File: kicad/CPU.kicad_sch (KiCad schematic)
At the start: 37 parts, among them J1 Conn_ARM_SWD_TagConnect_TC203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, J2 Screw_Terminal_01x03, J3 Screw_Terminal_01x03, SW1 SW_Push, U7 STM32F303CBTx, U8 ATA6560-GAQW-N, Y1 8 MHz

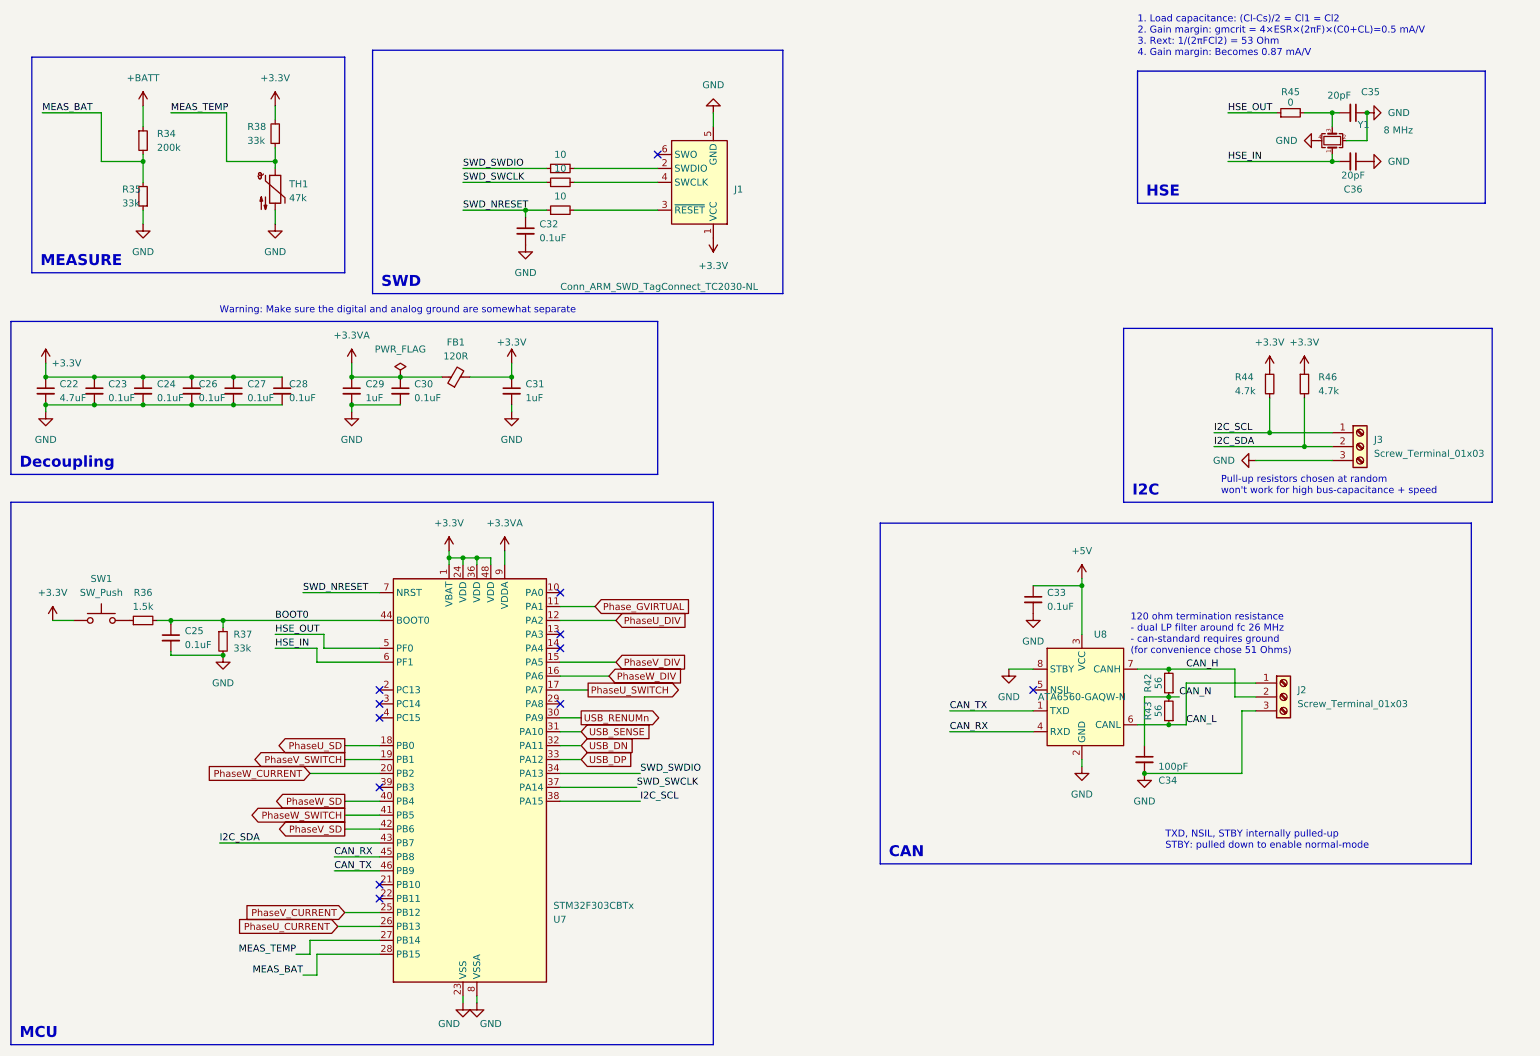
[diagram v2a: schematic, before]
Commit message: [kicad] Added different ESD protection device, silkscreen indication on the back, [review] Added pdf file and images of the front and back as well as 3d images
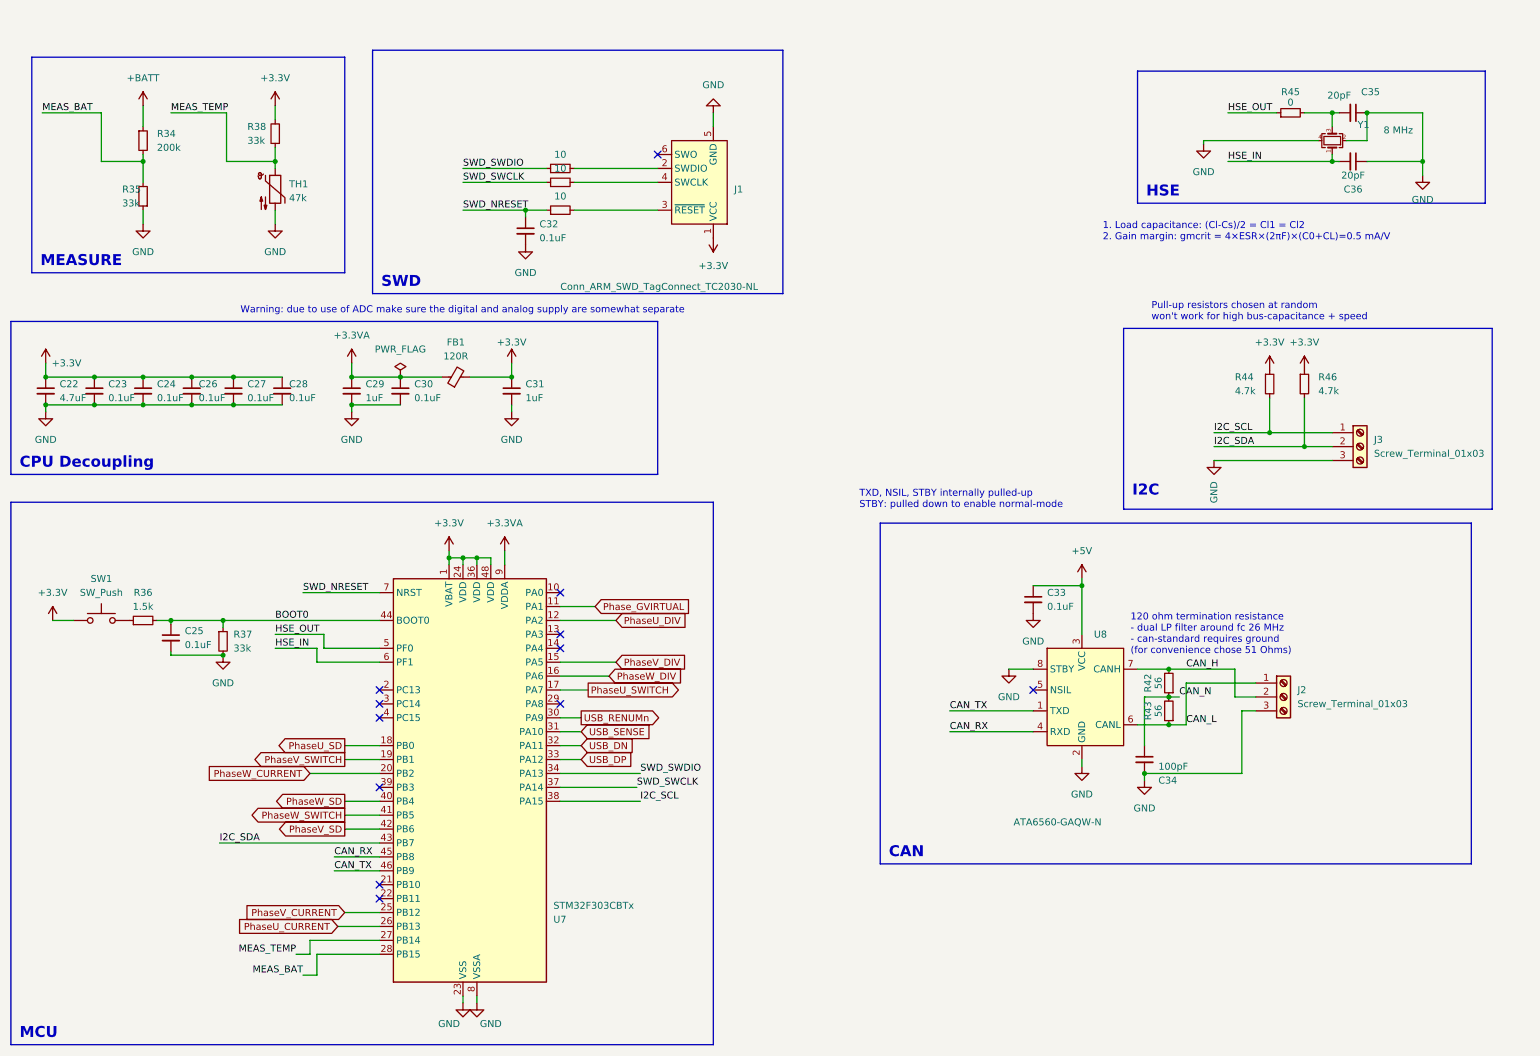
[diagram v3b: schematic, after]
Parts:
- R45: footprint Resistor_SMD:R_0402_1005Metric -> Resistor_SMD:R_0402_1005Metric_Pad0.72x0.64mm_HandSolder
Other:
- note added: "1. Load capacitance: (Cl-Cs)/2 = Cl1 = Cl2 2. Gain margin: gmcrit = 4×ESR×(2πF)×(C0+CL)=0.5 mA/V"
- note added: "Warning: due to use of ADC make sure the digital and analog supply are somewhat separate"
- note removed: "1. Load capacitance: (Cl-Cs)/2 = Cl1 = Cl2 2. Gain margin: gmcrit = 4×ESR×(2πF)×(C0+CL)=0.5 mA/V 3. Rext: 1/(2πFCl2) = 53 Ohm 4. Gain margin: Becomes 0.87 mA/V"
- note removed: "Warning: Make sure the digital and analog ground are somewhat separate"
- company: Igor Wolfs -> IW
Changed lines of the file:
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@@
     (title "BLDC Driver Project")
     (rev "1.0")
-    (company "Igor Wolfs")
+    (company "IW")
   )
   (junction (at 225.425 137.16) (diameter 0) (color 0 0 0 0)
+  )
+  (junction (at 271.78 34.29) (diameter 0) (color 0 0 0 0)
   )
   (junction (at 52.705 124.46) (diameter 0) (color 0 0 0 0)
@@
     (stroke (width 0) (type default))
   )
+  (wire (pts (xy 271.78 34.29) (xy 271.78 25.4))
+    (stroke (width 0) (type default))
+  )
   (wire (pts (xy 255.27 34.29) (xy 255.27 33.02))
     (stroke (width 0) (type default))
@@
     (stroke (width 0) (type default))
   )
+  (wire (pts (xy 231.775 30.48) (xy 231.775 31.115))
+    (stroke (width 0) (type default))
+  )
   (wire (pts (xy 243.84 83.82) (xy 255.27 83.82))
     (stroke (width 0) (type default))
@@
     (stroke (width 0) (type default))
   )
-  (wire (pts (xy 241.3 88.9) (xy 255.27 88.9))
+  (wire (pts (xy 233.68 88.9) (xy 255.27 88.9))
     (stroke (width 0) (type default))
   )
@@
     (stroke (width 0) (type default))
   )
+  (wire (pts (xy 271.78 25.4) (xy 261.62 25.4))
+    (stroke (width 0) (type default))
+  )
   (wire (pts (xy 38.1 73.66) (xy 46.99 73.66))
     (stroke (width 0) (type default))
@@
     (stroke (width 0) (type default))
   )
+  (wire (pts (xy 261.62 34.29) (xy 271.78 34.29))
+    (stroke (width 0) (type default))
+  )
   (wire (pts (xy 53.34 25.4) (xy 53.34 34.29))
     (stroke (width 0) (type default))
@@
     (stroke (width 0) (type default))
   )
+  (wire (pts (xy 271.78 36.83) (xy 271.78 34.29))
+    (stroke (width 0) (type default))
+  )
   (wire (pts (xy 68.58 179.07) (xy 66.04 179.07))
     (stroke (width 0) (type default))
@@
     (stroke (width 0) (type default))
   )
+  (wire (pts (xy 231.775 30.48) (xy 252.73 30.48))
+    (stroke (width 0) (type default))
+  )
   (wire (pts (xy 209.55 110.49) (xy 209.55 111.76))
     (stroke (width 0) (type default))
@@
     (stroke (width 0) (type default))
   )
+  (wire (pts (xy 220.98 147.32) (xy 220.98 146.05))
+    (stroke (width 0) (type default))
+  )
   (wire (pts (xy 74.93 156.21) (xy 81.28 156.21))
     (stroke (width 0) (type default))
@@
     (fill (type none))
   )
-  (rectangle (start 217.17 64.77) (end 284.48 96.52)
+  (rectangle (start 217.17 64.77) (end 284.48 97.79)
     (stroke (width 0) (type default))
     (fill (type none))
@@
     (effects (font (size 2 2) (thickness 2) bold) (justify left top))
   )
-  (text_box "Decoupling\n"
-    (at 13.97 86.36 0) (size 20.32 5.08)
+  (text_box "CPU Decoupling\n"
+    (at 13.97 86.36 0) (size 35.56 5.08)
     (stroke (width -0.0001) (type default))
     (fill (type none))
@@
   )
   (text "TXD, NSIL, STBY internally pulled-up\nSTBY: pulled down to enable normal-mode"
-    (at 224.79 160.02 0)
+    (at 168.91 97.79 0)
     (effects (font (size 1.27 1.27)) (justify left bottom))
   )
   (text "Pull-up resistors chosen at random\nwon't work for high bus-capacitance + speed"
-    (at 234.95 95.25 0)
-    (effects (font (size 1.27 1.27)) (justify left bottom))
-  )
-  (text "1. Load capacitance: (Cl-Cs)/2 = Cl1 = Cl2\n2. Gain margin: gmcrit = 4×ESR×(2πF)×(C0+CL)=0.5 mA/V\n3. Rext: 1/(2πFCl2) = 53 Ohm\n4. Gain margin: Becomes 0.87 mA/V\n"
-    (at 219.71 15.24 0)
-    (effects (font (size 1.27 1.27)) (justify left bottom))
-  )
-  (text "Warning: Make sure the digital and analog ground are somewhat separate\n"
-    (at 52.07 62.23 0)
+    (at 222.25 63.5 0)
+    (effects (font (size 1.27 1.27)) (justify left bottom))
+  )
+  (text "1. Load capacitance: (Cl-Cs)/2 = Cl1 = Cl2\n2. Gain margin: gmcrit = 4×ESR×(2πF)×(C0+CL)=0.5 mA/V"
+    (at 213.36 48.895 0)
+    (effects (font (size 1.27 1.27)) (justify left bottom))
+  )
+  (text "Warning: due to use of ADC make sure the digital and analog supply are somewhat separate\n"
+    (at 55.88 62.23 0)
     (effects (font (size 1.27 1.27)) (justify left bottom))
   )
@@
     )
   )
-  (symbol (lib_id "power:GND") (at 241.3 88.9 270) (unit 1)
+  (symbol (lib_id "power:GND") (at 233.68 88.9 0) (unit 1)
     (in_bom yes) (on_board yes) (dnp no)
-    (property "Reference" "#PWR053" (at 234.95 88.9 0)
-      (effects (font (size 1.27 1.27)) hide)
-    )
-    (property "Value" "GND" (at 237.49 88.9 90)
+    (property "Reference" "#PWR053" (at 233.68 95.25 0)
+      (effects (font (size 1.27 1.27)) hide)
+    )
+    (property "Value" "GND" (at 233.68 92.71 90)
       (effects (font (size 1.27 1.27)) (justify right))
     )
-    (property "Footprint" "" (at 241.3 88.9 0)
-      (effects (font (size 1.27 1.27)) hide)
-    )
-    (property "Datasheet" "" (at 241.3 88.9 0)
+    (property "Footprint" "" (at 233.68 88.9 0)
+      (effects (font (size 1.27 1.27)) hide)
+    )
+    (property "Datasheet" "" (at 233.68 88.9 0)
       (effects (font (size 1.27 1.27)) hide)
     )
@@
     )
   )
-  (symbol (lib_id "power:GND") (at 220.98 146.05 0) (unit 1)
-    (in_bom yes) (on_board yes) (dnp no) (fields_autoplaced)
-    (property "Reference" "#PWR052" (at 220.98 152.4 0)
-      (effects (font (size 1.27 1.27)) hide)
-    )
-    (property "Value" "GND" (at 220.98 151.13 0)
-      (effects (font (size 1.27 1.27)))
-    )
-    (property "Footprint" "" (at 220.98 146.05 0)
-      (effects (font (size 1.27 1.27)) hide)
-    )
-    (property "Datasheet" "" (at 220.98 146.05 0)
+  (symbol (lib_id "power:GND") (at 220.98 147.32 0) (unit 1)
+    (in_bom yes) (on_board yes) (dnp no) (fields_autoplaced)
+    (property "Reference" "#PWR052" (at 220.98 153.67 0)
+      (effects (font (size 1.27 1.27)) hide)
+    )
+    (property "Value" "GND" (at 220.98 152.4 0)
+      (effects (font (size 1.27 1.27)))
+    )
+    (property "Footprint" "" (at 220.98 147.32 0)
+      (effects (font (size 1.27 1.27)) hide)
+    )
+    (property "Datasheet" "" (at 220.98 147.32 0)
       (effects (font (size 1.27 1.27)) hide)
     )
@@
   )
   (symbol (lib_id "bldc:ATA6560") (at 209.55 132.08 0) (unit 1)
-    (in_bom yes) (on_board yes) (dnp no) (fields_autoplaced)
+    (in_bom yes) (on_board yes) (dnp no)
     (property "Reference" "U8" (at 211.7441 120.65 0)
       (effects (font (size 1.27 1.27)) (justify left))
     )
-    (property "Value" "ATA6560-GAQW-N" (at 209.55 132.08 0)
+    (property "Value" "ATA6560-GAQW-N" (at 205.105 154.94 0)
       (effects (font (size 1.27 1.27)))
     )
@@
     )
   )
-  (symbol (lib_id "power:GND") (at 261.62 25.4 90) (unit 1)
-    (in_bom yes) (on_board yes) (dnp no) (fields_autoplaced)
-    (property "Reference" "#PWR057" (at 267.97 25.4 0)
-      (effects (font (size 1.27 1.27)) hide)
-    )
-    (property "Value" "GND" (at 265.43 25.4 90)
-      (effects (font (size 1.27 1.27)) (justify right))
-    )
-    (property "Footprint" "" (at 261.62 25.4 0)
-      (effects (font (size 1.27 1.27)) hide)
-    )
-    (property "Datasheet" "" (at 261.62 25.4 0)
+  (symbol (lib_id "power:GND") (at 271.78 36.83 0) (unit 1)
+    (in_bom yes) (on_board yes) (dnp no) (fields_autoplaced)
+    (property "Reference" "#PWR057" (at 271.78 43.18 0)
+      (effects (font (size 1.27 1.27)) hide)
+    )
+    (property "Value" "GND" (at 271.78 41.275 0)
+      (effects (font (size 1.27 1.27)))
+    )
+    (property "Footprint" "" (at 271.78 36.83 0)
+      (effects (font (size 1.27 1.27)) hide)
+    )
+    (property "Datasheet" "" (at 271.78 36.83 0)
       (effects (font (size 1.27 1.27)) hide)
     )
@@
     )
   )
-  (symbol (lib_id "power:GND") (at 252.73 30.48 270) (unit 1)
-    (in_bom yes) (on_board yes) (dnp no) (fields_autoplaced)
-    (property "Reference" "#PWR056" (at 246.38 30.48 0)
-      (effects (font (size 1.27 1.27)) hide)
-    )
-    (property "Value" "GND" (at 248.92 30.48 90)
-      (effects (font (size 1.27 1.27)) (justify right))
-    )
-    (property "Footprint" "" (at 252.73 30.48 0)
-      (effects (font (size 1.27 1.27)) hide)
-    )
-    (property "Datasheet" "" (at 252.73 30.48 0)
+  (symbol (lib_id "power:GND") (at 231.775 31.115 0) (unit 1)
+    (in_bom yes) (on_board yes) (dnp no) (fields_autoplaced)
+    (property "Reference" "#PWR056" (at 231.775 37.465 0)
+      (effects (font (size 1.27 1.27)) hide)
+    )
+    (property "Value" "GND" (at 231.775 36.195 0)
+      (effects (font (size 1.27 1.27)))
+    )
+    (property "Footprint" "" (at 231.775 31.115 0)
+      (effects (font (size 1.27 1.27)) hide)
+    )
+    (property "Datasheet" "" (at 231.775 31.115 0)
       (effects (font (size 1.27 1.27)) hide)
     )
@@
     )
   )
-  (symbol (lib_id "power:GND") (at 261.62 34.29 90) (unit 1)
-    (in_bom yes) (on_board yes) (dnp no) (fields_autoplaced)
-    (property "Reference" "#PWR058" (at 267.97 34.29 0)
-      (effects (font (size 1.27 1.27)) hide)
-    )
-    (property "Value" "GND" (at 265.43 34.29 90)
-      (effects (font (size 1.27 1.27)) (justify right))
-    )
-    (property "Footprint" "" (at 261.62 34.29 0)
-      (effects (font (size 1.27 1.27)) hide)
-    )
-    (property "Datasheet" "" (at 261.62 34.29 0)
-      (effects (font (size 1.27 1.27)) hide)
-    )
-    (pin "1")
-    (instances
-      (project "bldc_project"
-        (path "/91e2f46a-700b-4d7a-a06a-22469f63223f/7eb1e86b-8a48-408f-b231-0c52f4ea1971"
-          (reference "#PWR058") (unit 1)
-        )
-      )
-    )
-  )
   (symbol (lib_id "power:GND") (at 142.24 25.4 180) (unit 1)
     (in_bom yes) (on_board yes) (dnp no) (fields_autoplaced)
@@
       (effects (font (size 1.27 1.27)))
     )
-    (property "Footprint" "Resistor_SMD:R_0402_1005Metric" (at 247.65 25.4 0)
-      (effects (font (size 1.27 1.27)) hide)
-    )
+    (property "Footprint" "Resistor_SMD:R_0402_1005Metric_Pad0.72x0.64mm_HandSolder" (at 247.65 25.4 0)
+      (effects (font (size 1.27 1.27)) hide)
+    )

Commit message: minor change
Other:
- note added: "120 ohm termination resistance - dual LP filter around fc 26 MHz - can-standard requires ground (for convenience chose 56 Ohms)"
- note removed: "120 ohm termination resistance - dual LP filter around fc 26 MHz - can-standard requires ground (for convenience chose 51 Ohms)"
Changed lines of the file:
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@@
     (effects (font (size 1.27 1.27)) (justify left bottom))
   )
-  (text "120 ohm termination resistance\n- dual LP filter around fc 26 MHz\n- can-standard requires ground\n(for convenience chose 51 Ohms)"
+  (text "120 ohm termination resistance\n- dual LP filter around fc 26 MHz\n- can-standard requires ground\n(for convenience chose 56 Ohms)"
     (at 218.44 124.46 0)
     (effects (font (size 1.27 1.27)) (justify left bottom))
